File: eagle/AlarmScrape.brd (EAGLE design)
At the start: 67.9 x 20.3 mm, 24 parts, among them IC1 LM339D, Q2 POW-EBAY, SW1 TACTILE-2, T1 2222, X1 POW, X2 Z12, X3 Z34

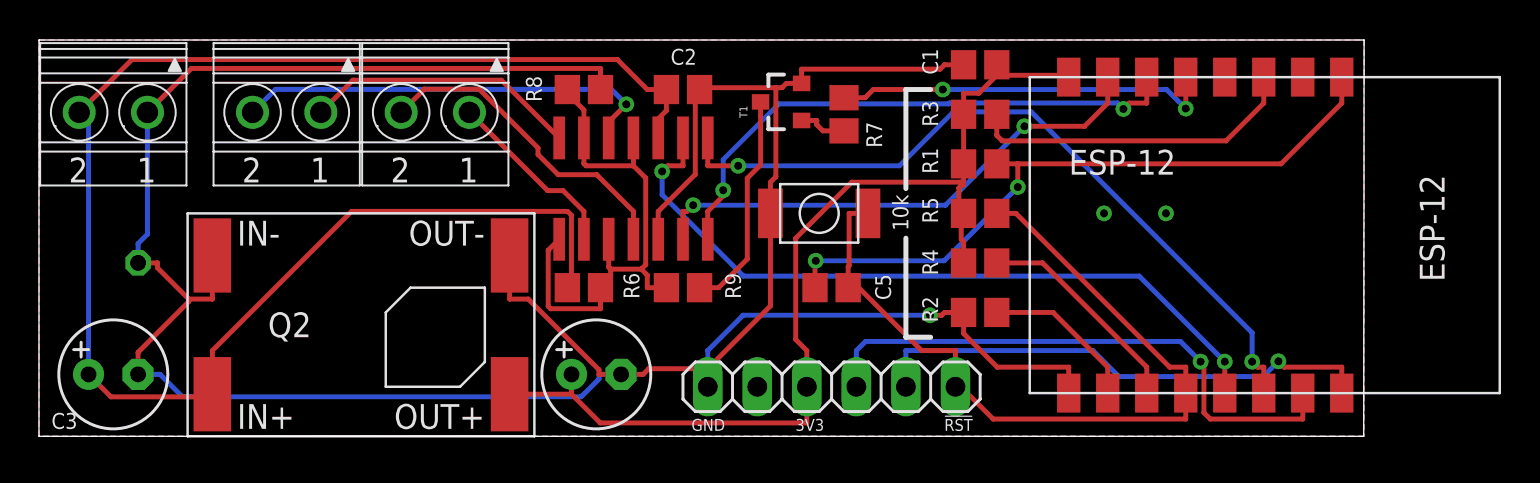
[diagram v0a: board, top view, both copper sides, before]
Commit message: PCB rev 2
-- Added LED
-- Removed !RESET pullup
-- Disconnected RTS from GP0 and !RESET
-- FTDI VCC now connected to VIN instead of 3.3V
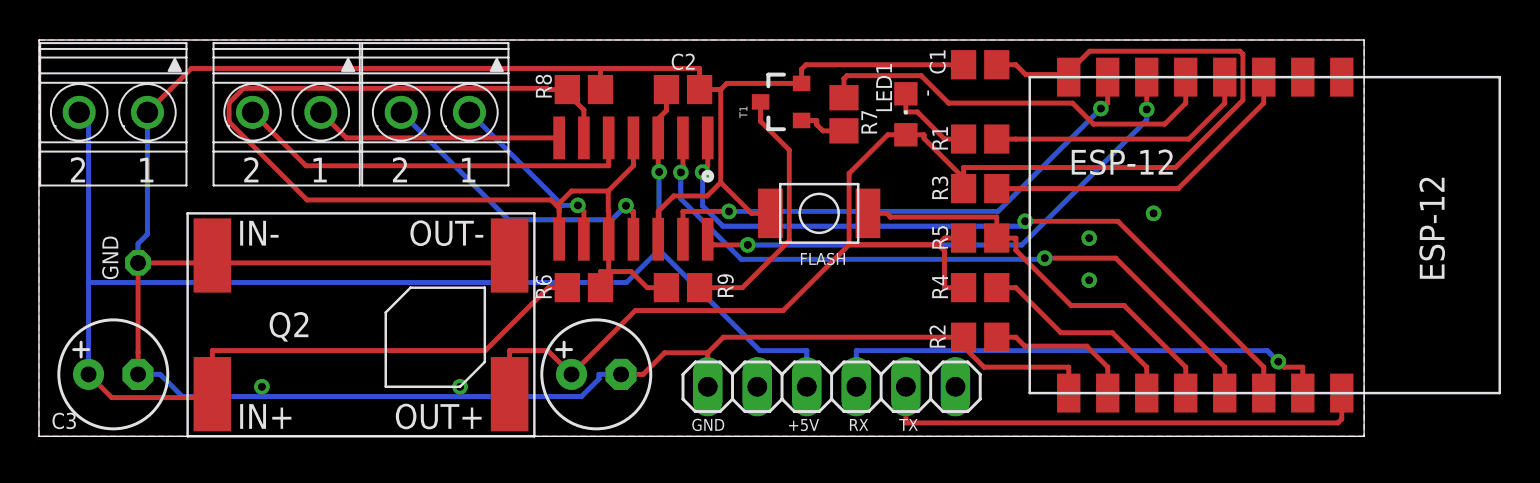
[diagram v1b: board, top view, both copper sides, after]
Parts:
- removed C5: 0.1u, resistor:C0805
- added LED1: (no value), led:CHIPLED_0805
- R1: value 10k -> 470
- SW1: value TACTILE-2 -> FLASH
- moved R3 3.81 mm to (48.3, 12.7)
- moved R4 1.27 mm to (48.3, 7.62)
- moved R1 1.27 mm to (48.3, 15.2)
- moved R2 1.27 mm to (48.3, 5.08)
- moved R5 1.27 mm to (48.3, 10.2)
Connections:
- removed net !PROG: C5.1, ESP-12.4, JP1.6, R5.1, SW1.P1
- removed net !RST: C5.2, ESP-12.9, R1.1
- new net !FLASH: ESP-12.4, R5.1, SW1.P1
- new net N$1: ESP-12.12, R1.1
- new net N$4: LED1.C, R1.2
- net +3V3: now also LED1.A; no longer JP1.3, R1.2
- net VCC: now also JP1.3
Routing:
- net !PROG: track 41.9 -> 0.00 mm
- net !RST: track 34.8 -> 0.00 mm, vias 2 -> 0
- net N$7: track 27.7 -> 56.7 mm
- net +3V3: track 51.9 -> 76.4 mm
- net !FLASH: track 0.00 -> 21.9 mm
- net N$1: track 0.00 -> 13.8 mm
- net VCC: track 82.5 -> 92.3 mm, vias 0 -> 1
- net N$4: track 0.00 -> 4.47 mm
- net TX: track 29.4 -> 26.4 mm
- net GND: track 149.4 -> 146.6 mm, vias 3 -> 5
- net N$8: track 11.4 -> 13.3 mm
- net ZONE2: track 37.8 -> 36.0 mm
- net C_REF: track 19.7 -> 21.4 mm, vias 2 -> 0
- net ZONE3: track 28.9 -> 27.5 mm
- net ZONE1: track 38.7 -> 37.3 mm
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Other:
- board text added: "+5V"
- board text added: "-"
- board text added: "AlarmSnoop v2"
- board text added: "FLASH"
- board text added: "RX"
- board text added: "TX"
- board text removed: "!RST"
- board text removed: "10k"
- board text removed: "3V3"
- board text removed: "AlarmSnoop v1"
